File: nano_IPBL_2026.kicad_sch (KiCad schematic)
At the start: 23 parts, among them J3 DB301V-5.0-2P, M1+ Motor_Servo, M10+ Motor_Servo, M11+ Motor_Servo, M12+ Motor_Servo, M2+ Motor_Servo, M3+ Motor_Servo, M4+ Motor_Servo, M5+ Motor_Servo, M6+ Motor_Servo, M7+ Motor_Servo, M8+ Motor_Servo, M9+ Motor_Servo

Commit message: Adjust track width and copper clearance, match solder mask to copper pad width
Update silkscreen text and drill hole visibility on B_Cu/F_Silkscreen layers.
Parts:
- renumbered M1+ to M1+1, M10+ to M10+1, M11+ to M11+1, M12+ to M12+1, M2+ to M2+1, M3+ to M3+1, M4+ to M4+1, M5+ to M5+1, M6+ to M6+1, M7+ to M7+1, M8+ to M8+1, M9+ to M9+1
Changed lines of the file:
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@@
 		(in_pos_files yes)
 		(dnp no)
-		(property "Reference" "M4+"
+		(property "Reference" "M4+1"
 			(at 72.898 147.828 0)
 			(show_name no)
@@
 			(project "nano_IPBL_2026"
 				(path "/0d35483a-0b12-46cc-b9f2-896fd6831779"
-					(reference "M4+")
+					(reference "M4+1")
 					(unit 1)
 				)
@@
 		(dnp no)
 		(fields_autoplaced yes)
-		(property "Reference" "M10+"
+		(property "Reference" "M10+1"
 			(at 146.05 124.0268 0)
 			(show_name no)
@@
 			(project "nano_IPBL_2026"
 				(path "/0d35483a-0b12-46cc-b9f2-896fd6831779"
-					(reference "M10+")
+					(reference "M10+1")
 					(unit 1)
 				)
@@
 		(in_pos_files yes)
 		(dnp no)
-		(property "Reference" "M1+"
+		(property "Reference" "M1+1"
 			(at 72.898 104.902 0)
 			(show_name no)
@@
 			(project "nano_IPBL_2026"
 				(path "/0d35483a-0b12-46cc-b9f2-896fd6831779"
-					(reference "M1+")
+					(reference "M1+1")
 					(unit 1)
 				)
@@
 		(dnp no)
 		(fields_autoplaced yes)
-		(property "Reference" "M9+"
+		(property "Reference" "M9+1"
 			(at 146.05 110.0568 0)
 			(show_name no)
@@
 			(project "nano_IPBL_2026"
 				(path "/0d35483a-0b12-46cc-b9f2-896fd6831779"
-					(reference "M9+")
+					(reference "M9+1")
 					(unit 1)
 				)
@@
 		(in_pos_files yes)
 		(dnp no)
-		(property "Reference" "M6+"
+		(property "Reference" "M6+1"
 			(at 104.648 118.872 0)
 			(show_name no)
@@
 			(project "nano_IPBL_2026"
 				(path "/0d35483a-0b12-46cc-b9f2-896fd6831779"
-					(reference "M6+")
+					(reference "M6+1")
 					(unit 1)
 				)
@@
 		(in_pos_files yes)
 		(dnp no)
-		(property "Reference" "M5+"
+		(property "Reference" "M5+1"
 			(at 104.648 105.156 0)
 			(show_name no)
@@
 			(project "nano_IPBL_2026"
 				(path "/0d35483a-0b12-46cc-b9f2-896fd6831779"
-					(reference "M5+")
+					(reference "M5+1")
 					(unit 1)
 				)
@@
 		(dnp no)
 		(fields_autoplaced yes)
-		(property "Reference" "M11+"
+		(property "Reference" "M11+1"
 			(at 146.05 137.9968 0)
 			(show_name no)
@@
 			(project "nano_IPBL_2026"
 				(path "/0d35483a-0b12-46cc-b9f2-896fd6831779"
-					(reference "M11+")
+					(reference "M11+1")
 					(unit 1)
 				)
@@
 		(in_pos_files yes)
 		(dnp no)
-		(property "Reference" "M7+"
+		(property "Reference" "M7+1"
 			(at 104.648 133.096 0)
 			(show_name no)
@@
 			(project "nano_IPBL_2026"
 				(path "/0d35483a-0b12-46cc-b9f2-896fd6831779"
-					(reference "M7+")
+					(reference "M7+1")
 					(unit 1)
 				)
@@
 		(in_pos_files yes)
 		(dnp no)
-		(property "Reference" "M3+"
+		(property "Reference" "M3+1"
 			(at 72.898 133.096 0)
 			(show_name no)
@@
 			(project "nano_IPBL_2026"
 				(path "/0d35483a-0b12-46cc-b9f2-896fd6831779"
-					(reference "M3+")
+					(reference "M3+1")
 					(unit 1)
 				)
@@
 		(dnp no)
 		(fields_autoplaced yes)
-		(property "Reference" "M12+"
+		(property "Reference" "M12+1"
 			(at 146.05 153.2368 0)
 			(show_name no)
@@
 			(project "nano_IPBL_2026"
 				(path "/0d35483a-0b12-46cc-b9f2-896fd6831779"
-					(reference "M12+")
+					(reference "M12+1")
 					(unit 1)
 				)
@@
 		(in_pos_files yes)
 		(dnp no)
-		(property "Reference" "M2+"
+		(property "Reference" "M2+1"
 			(at 73.152 118.364 0)
 			(show_name no)
@@
 			(project "nano_IPBL_2026"
 				(path "/0d35483a-0b12-46cc-b9f2-896fd6831779"
-					(reference "M2+")
+					(reference "M2+1")
 					(unit 1)
 				)
@@
 		(in_pos_files yes)
 		(dnp no)
-		(property "Reference" "M8+"
+		(property "Reference" "M8+1"
 			(at 104.648 148.844 0)
 			(show_name no)
@@
 			(project "nano_IPBL_2026"
 				(path "/0d35483a-0b12-46cc-b9f2-896fd6831779"
-					(reference "M8+")
-					(unit 1)
-				)
+					(reference "M8+1")
+					(unit 1)
+				)

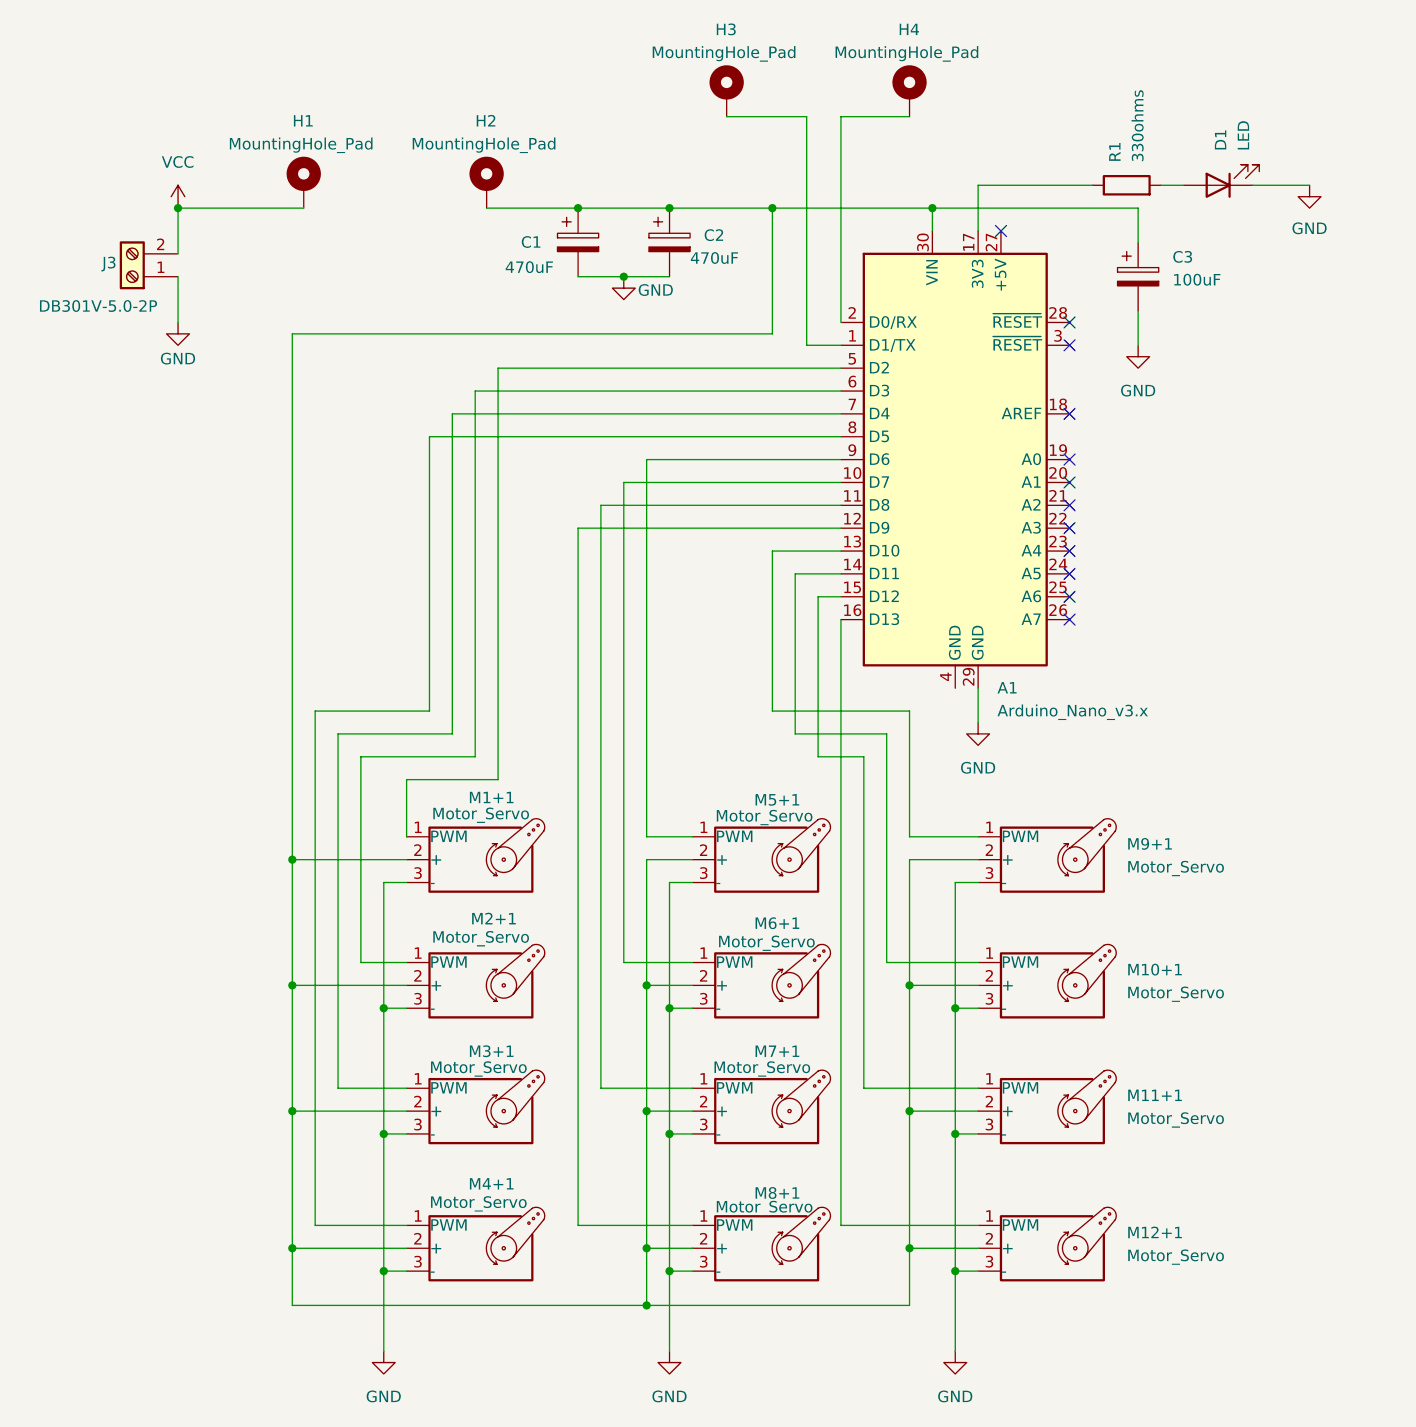
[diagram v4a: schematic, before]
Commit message: Update PCB design to revision 3.3 and schematic to revision 2.1
- Remove RX/TX mounting holes from schematic
- Prepare for servo pin net label updates
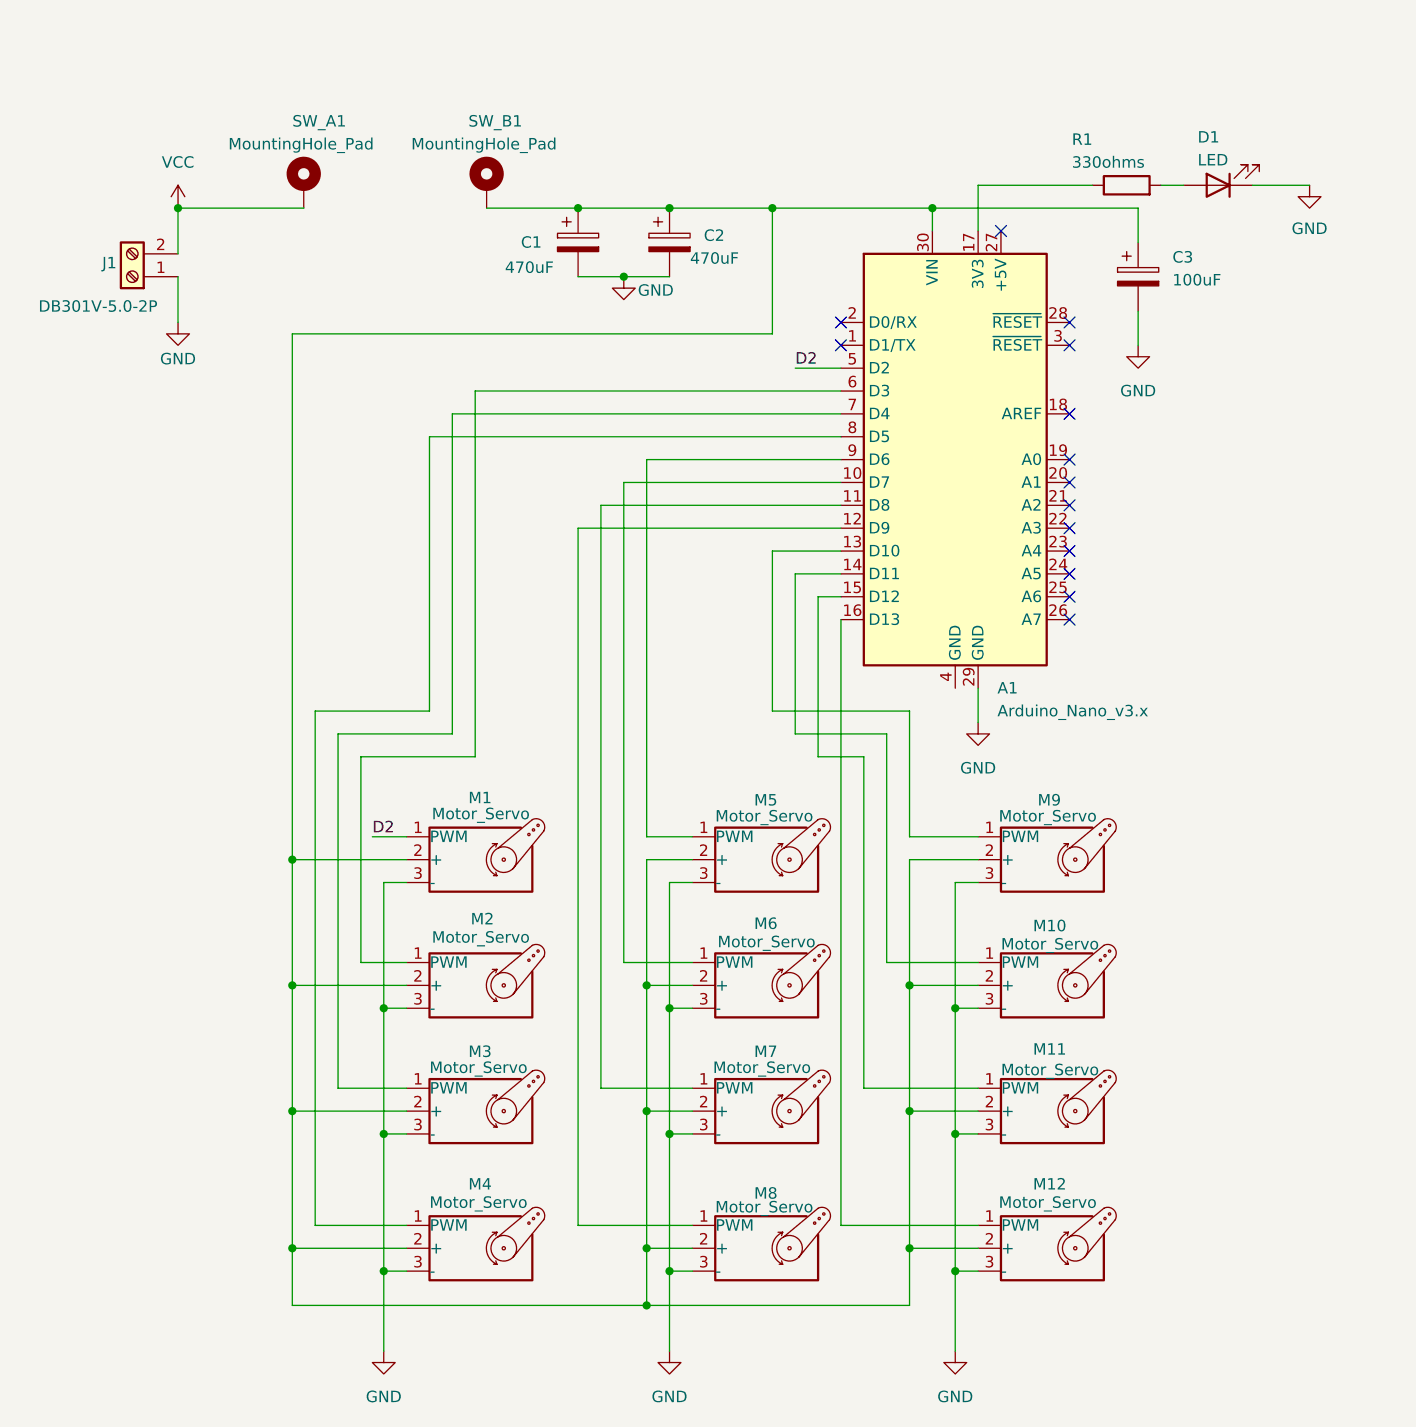
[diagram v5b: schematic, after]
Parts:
- removed H3, H4: MountingHole_Pad, Arduino_MountingHole:MountingHole_1.2mm_M2_Pad_EDITED, symbol Mechanical:MountingHole_Pad
- renumbered J3 to J1, M1+1 to M1, M10+1 to M10, M11+1 to M11, M12+1 to M12, M2+1 to M2, M3+1 to M3, M4+1 to M4, M5+1 to M5, M6+1 to M6, M7+1 to M7, M8+1 to M8, M9+1 to M9, H1 to SW_A1, H2 to SW_B1
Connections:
- net D2: now reaches A1.5 (D2), M1.1 (PWM)
- no-connect marks 12 -> 14
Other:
- title: (none) -> iPBL 2026 - Servo Nano Connection
